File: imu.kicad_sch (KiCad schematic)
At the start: 4 parts

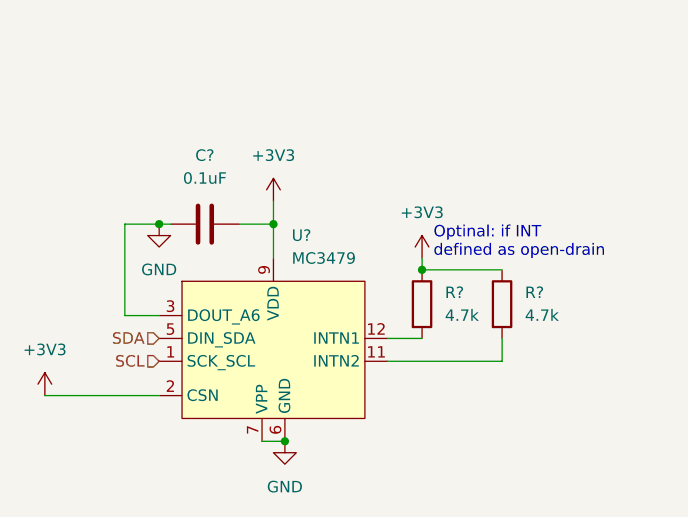
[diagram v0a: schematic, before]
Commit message: Added display, update lora sym, updated usb-pd schematic, connected sd, added external buttons
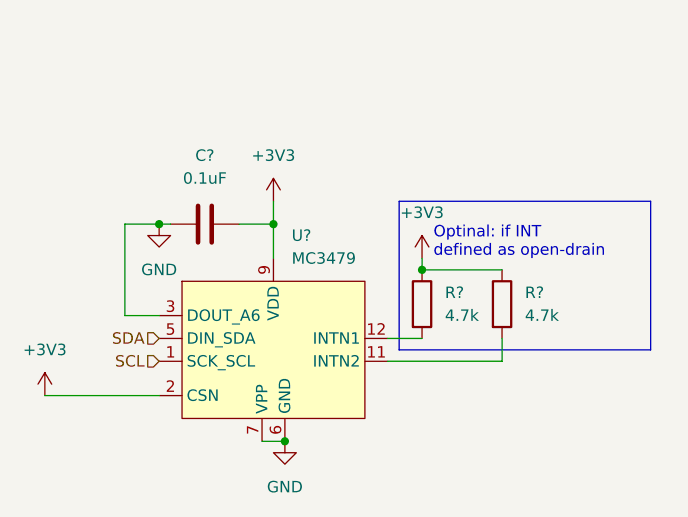
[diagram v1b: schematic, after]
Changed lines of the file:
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@@
+    (stroke (width 0) (type default) (color 0 0 0 0))
+  )
+  (polyline (pts (xy 154.94 81.28) (xy 182.88 81.28))
     (stroke (width 0) (type default) (color 0 0 0 0))
   )
@@
   )
   (wire (pts (xy 124.46 93.98) (xy 124.46 83.82))
+    (stroke (width 0) (type default) (color 0 0 0 0))
+  )
+  (polyline (pts (xy 154.94 81.28) (xy 154.94 97.79))
+    (stroke (width 0) (type default) (color 0 0 0 0))
+  )
+  (polyline (pts (xy 154.94 97.79) (xy 182.88 97.79))
     (stroke (width 0) (type default) (color 0 0 0 0))
   )
@@
     (stroke (width 0) (type default) (color 0 0 0 0))
   )
+  (polyline (pts (xy 182.88 97.79) (xy 182.88 81.28))
+    (stroke (width 0) (type default) (color 0 0 0 0))
+  )

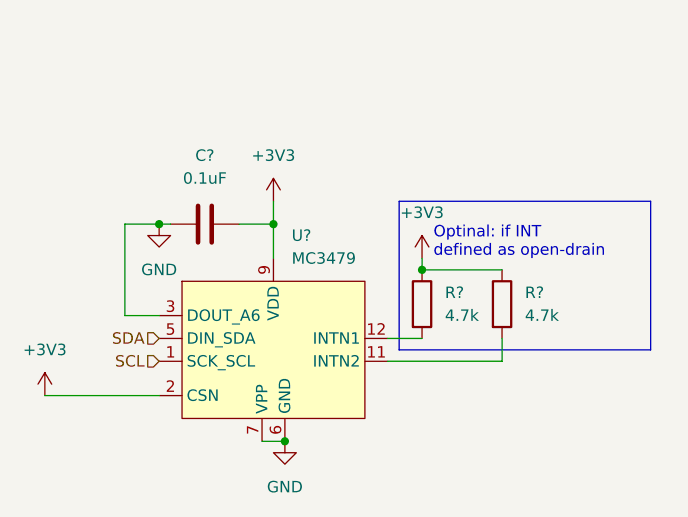
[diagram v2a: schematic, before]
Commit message: added audio ref schematic, added bat to 5V, added shift register, connected devices with other periferals
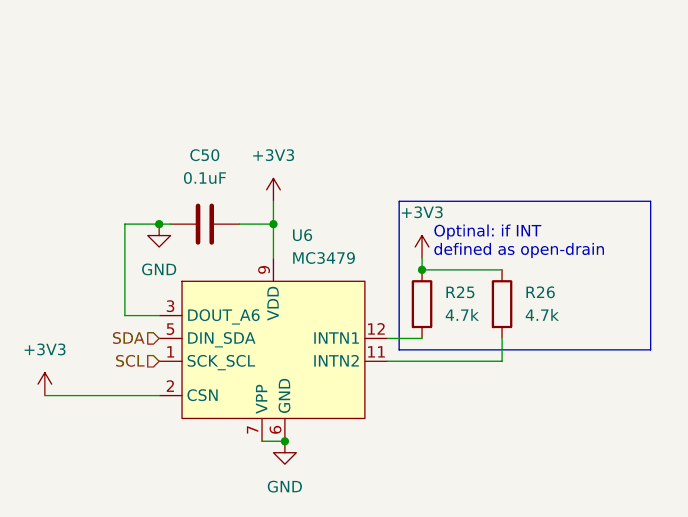
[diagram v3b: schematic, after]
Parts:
- gave numbers to parts that had none: 4
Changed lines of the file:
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@@
   (symbol (lib_id "Device:C") (at 133.35 83.82 90) (unit 1)
     (in_bom yes) (on_board yes) (fields_autoplaced)
-    (property "Reference" "C?" (id 0) (at 133.35 76.2 90))
+    (property "Reference" "C50" (id 0) (at 133.35 76.2 90))
     (property "Value" "0.1uF" (id 1) (at 133.35 78.74 90))
     (property "Footprint" "" (id 2) (at 137.16 82.8548 0)
@@
   (symbol (lib_id "Device:R") (at 157.48 92.71 0) (unit 1)
     (in_bom yes) (on_board yes) (fields_autoplaced)
-    (property "Reference" "R?" (id 0) (at 160.02 91.4399 0)
+    (property "Reference" "R25" (id 0) (at 160.02 91.4399 0)
       (effects (font (size 1.27 1.27)) (justify left))
     )
@@
   (symbol (lib_id "Device:R") (at 166.37 92.71 0) (unit 1)
     (in_bom yes) (on_board yes) (fields_autoplaced)
-    (property "Reference" "R?" (id 0) (at 168.91 91.4399 0)
+    (property "Reference" "R26" (id 0) (at 168.91 91.4399 0)
       (effects (font (size 1.27 1.27)) (justify left))
     )
@@
   (symbol (lib_id "airsoft_controller:MC3479") (at 140.97 97.79 0) (unit 1)
     (in_bom yes) (on_board yes) (fields_autoplaced)
-    (property "Reference" "U?" (id 0) (at 142.9894 85.09 0)
+    (property "Reference" "U6" (id 0) (at 142.9894 85.09 0)
       (effects (font (size 1.27 1.27)) (justify left))
     )

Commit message: added adcin2 config description, fixed some rule check errors
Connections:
- now unconnected: U6.10 (NC), U6.4 (NC), U6.8 (NC)

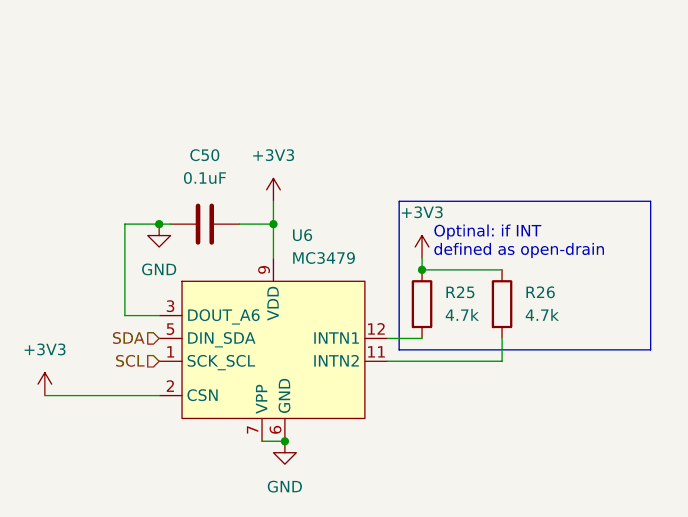
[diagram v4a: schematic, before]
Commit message: minor optimized pinassignement, added capacitors, added connectors
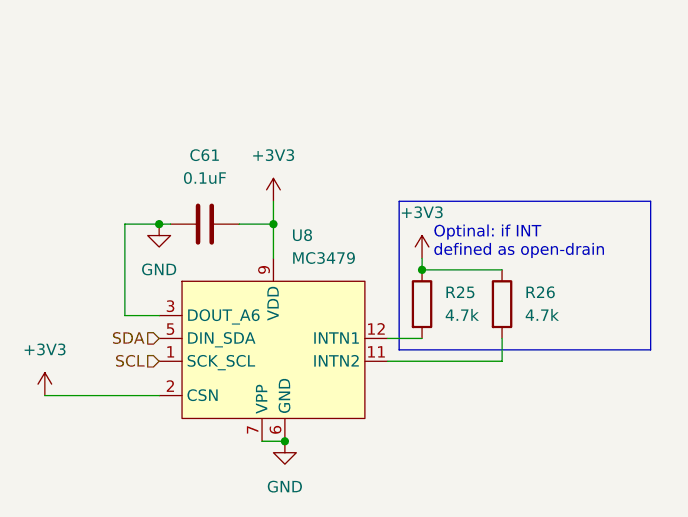
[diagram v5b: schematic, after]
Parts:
- renumbered C50 to C61, U6 to U8
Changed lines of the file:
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@@
   (symbol (lib_id "Device:C") (at 133.35 83.82 90) (unit 1)
     (in_bom yes) (on_board yes) (fields_autoplaced)
-    (property "Reference" "C50" (id 0) (at 133.35 76.2 90))
+    (property "Reference" "C61" (id 0) (at 133.35 76.2 90))
     (property "Value" "0.1uF" (id 1) (at 133.35 78.74 90))
     (property "Footprint" "" (id 2) (at 137.16 82.8548 0)
@@
   (symbol (lib_id "power:+3V3") (at 140.97 81.28 0) (unit 1)
     (in_bom yes) (on_board yes) (fields_autoplaced)
-    (property "Reference" "#PWR0152" (id 0) (at 140.97 85.09 0)
+    (property "Reference" "#PWR071" (id 0) (at 140.97 85.09 0)
       (effects (font (size 1.27 1.27)) hide)
     )
@@
   (symbol (lib_id "power:+3V3") (at 115.57 102.87 0) (unit 1)
     (in_bom yes) (on_board yes) (fields_autoplaced)
-    (property "Reference" "#PWR0155" (id 0) (at 115.57 106.68 0)
+    (property "Reference" "#PWR069" (id 0) (at 115.57 106.68 0)
       (effects (font (size 1.27 1.27)) hide)
     )
@@
   (symbol (lib_id "power:+3V3") (at 157.48 87.63 0) (unit 1)
     (in_bom yes) (on_board yes) (fields_autoplaced)
-    (property "Reference" "#PWR0154" (id 0) (at 157.48 91.44 0)
+    (property "Reference" "#PWR073" (id 0) (at 157.48 91.44 0)
       (effects (font (size 1.27 1.27)) hide)
     )
@@
   (symbol (lib_id "airsoft_controller:MC3479") (at 140.97 97.79 0) (unit 1)
     (in_bom yes) (on_board yes) (fields_autoplaced)
-    (property "Reference" "U6" (id 0) (at 142.9894 85.09 0)
+    (property "Reference" "U8" (id 0) (at 142.9894 85.09 0)
       (effects (font (size 1.27 1.27)) (justify left))
     )
@@
   (symbol (lib_id "power:GND") (at 128.27 83.82 0) (unit 1)
     (in_bom yes) (on_board yes) (fields_autoplaced)
-    (property "Reference" "#PWR0153" (id 0) (at 128.27 90.17 0)
+    (property "Reference" "#PWR070" (id 0) (at 128.27 90.17 0)
       (effects (font (size 1.27 1.27)) hide)
     )
@@
   (symbol (lib_id "power:GND") (at 142.24 107.95 0) (unit 1)
     (in_bom yes) (on_board yes) (fields_autoplaced)
-    (property "Reference" "#PWR0156" (id 0) (at 142.24 114.3 0)
+    (property "Reference" "#PWR072" (id 0) (at 142.24 114.3 0)
       (effects (font (size 1.27 1.27)) hide)
     )

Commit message: PI LC lowpass filter, added CP2012 reset, added connectors
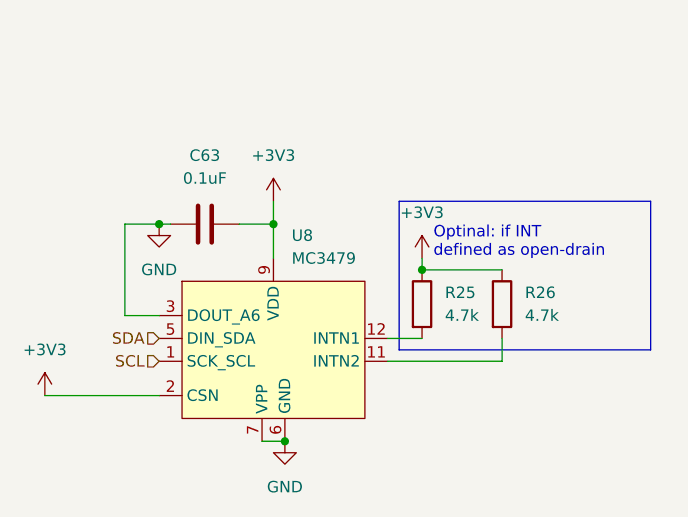
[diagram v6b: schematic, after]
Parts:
- renumbered C61 to C63
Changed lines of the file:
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@@
   (symbol (lib_id "Device:C") (at 133.35 83.82 90) (unit 1)
     (in_bom yes) (on_board yes) (fields_autoplaced)
-    (property "Reference" "C61" (id 0) (at 133.35 76.2 90))
+    (property "Reference" "C63" (id 0) (at 133.35 76.2 90))
     (property "Value" "0.1uF" (id 1) (at 133.35 78.74 90))
     (property "Footprint" "" (id 2) (at 137.16 82.8548 0)
@@
   (symbol (lib_id "power:+3V3") (at 140.97 81.28 0) (unit 1)
     (in_bom yes) (on_board yes) (fields_autoplaced)
-    (property "Reference" "#PWR071" (id 0) (at 140.97 85.09 0)
+    (property "Reference" "#PWR070" (id 0) (at 140.97 85.09 0)
       (effects (font (size 1.27 1.27)) hide)
     )
@@
   (symbol (lib_id "power:+3V3") (at 115.57 102.87 0) (unit 1)
     (in_bom yes) (on_board yes) (fields_autoplaced)
-    (property "Reference" "#PWR069" (id 0) (at 115.57 106.68 0)
+    (property "Reference" "#PWR068" (id 0) (at 115.57 106.68 0)
       (effects (font (size 1.27 1.27)) hide)
     )
@@
   (symbol (lib_id "power:+3V3") (at 157.48 87.63 0) (unit 1)
     (in_bom yes) (on_board yes) (fields_autoplaced)
-    (property "Reference" "#PWR073" (id 0) (at 157.48 91.44 0)
+    (property "Reference" "#PWR072" (id 0) (at 157.48 91.44 0)
       (effects (font (size 1.27 1.27)) hide)
     )
@@
   (symbol (lib_id "power:GND") (at 128.27 83.82 0) (unit 1)
     (in_bom yes) (on_board yes) (fields_autoplaced)
-    (property "Reference" "#PWR070" (id 0) (at 128.27 90.17 0)
+    (property "Reference" "#PWR069" (id 0) (at 128.27 90.17 0)
       (effects (font (size 1.27 1.27)) hide)
     )
@@
   (symbol (lib_id "power:GND") (at 142.24 107.95 0) (unit 1)
     (in_bom yes) (on_board yes) (fields_autoplaced)
-    (property "Reference" "#PWR072" (id 0) (at 142.24 114.3 0)
+    (property "Reference" "#PWR071" (id 0) (at 142.24 114.3 0)
       (effects (font (size 1.27 1.27)) hide)
     )

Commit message: added nfc antenna components, added most of footprints
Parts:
- C63: footprint (none) -> Capacitor_SMD:C_0603_1608Metric_Pad1.08x0.95mm_HandSolder
- R25, R26: footprint (none) -> Resistor_SMD:R_0603_1608Metric_Pad0.98x0.95mm_HandSolder
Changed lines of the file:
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@@
     (property "Reference" "C63" (id 0) (at 133.35 76.2 90))
     (property "Value" "0.1uF" (id 1) (at 133.35 78.74 90))
-    (property "Footprint" "" (id 2) (at 137.16 82.8548 0)
+    (property "Footprint" "Capacitor_SMD:C_0603_1608Metric_Pad1.08x0.95mm_HandSolder" (id 2) (at 137.16 82.8548 0)
       (effects (font (size 1.27 1.27)) hide)
     )
@@
       (effects (font (size 1.27 1.27)) (justify left))
     )
-    (property "Footprint" "" (id 2) (at 155.702 92.71 90)
+    (property "Footprint" "Resistor_SMD:R_0603_1608Metric_Pad0.98x0.95mm_HandSolder" (id 2) (at 155.702 92.71 90)
       (effects (font (size 1.27 1.27)) hide)
     )
@@
       (effects (font (size 1.27 1.27)) (justify left))
     )
-    (property "Footprint" "" (id 2) (at 164.592 92.71 90)
+    (property "Footprint" "Resistor_SMD:R_0603_1608Metric_Pad0.98x0.95mm_HandSolder" (id 2) (at 164.592 92.71 90)
       (effects (font (size 1.27 1.27)) hide)
     )

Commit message: schematic creation
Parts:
- renumbered C63 to C65, R25 to R23, R26 to R24
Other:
- moved on the sheet: C65
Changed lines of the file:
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@@
   (junction (at 157.48 88.9) (diameter 0) (color 0 0 0 0)
   )
-  (junction (at 140.97 83.82) (diameter 0) (color 0 0 0 0)
-  )
-  (junction (at 128.27 83.82) (diameter 0) (color 0 0 0 0)
-  )
   (junction (at 142.24 107.95) (diameter 0) (color 0 0 0 0)
   )
-  (wire (pts (xy 140.97 83.82) (xy 140.97 87.63))
-    (stroke (width 0) (type default) (color 0 0 0 0))
-  )
-  (wire (pts (xy 137.16 83.82) (xy 140.97 83.82))
+  (wire (pts (xy 140.97 86.36) (xy 140.97 87.63))
     (stroke (width 0) (type default) (color 0 0 0 0))
   )
@@
     (stroke (width 0) (type default) (color 0 0 0 0))
   )
-  (wire (pts (xy 124.46 83.82) (xy 128.27 83.82))
-    (stroke (width 0) (type default) (color 0 0 0 0))
-  )
-  (wire (pts (xy 124.46 93.98) (xy 124.46 83.82))
-    (stroke (width 0) (type default) (color 0 0 0 0))
-  )
   (wire (pts (xy 153.67 96.52) (xy 157.48 96.52))
     (stroke (width 0) (type default) (color 0 0 0 0))
@@
     (stroke (width 0) (type default) (color 0 0 0 0))
   )
-  (wire (pts (xy 140.97 81.28) (xy 140.97 83.82))
+  (wire (pts (xy 128.27 87.63) (xy 128.27 93.98))
     (stroke (width 0) (type default) (color 0 0 0 0))
   )
@@
     (stroke (width 0) (type default) (color 0 0 0 0))
   )
-  (wire (pts (xy 128.27 83.82) (xy 129.54 83.82))
-    (stroke (width 0) (type default) (color 0 0 0 0))
-  )
   (wire (pts (xy 139.7 107.95) (xy 142.24 107.95))
     (stroke (width 0) (type default) (color 0 0 0 0))
   )
-  (wire (pts (xy 128.27 93.98) (xy 124.46 93.98))
+  (wire (pts (xy 115.57 87.63) (xy 128.27 87.63))
     (stroke (width 0) (type default) (color 0 0 0 0))
   )
@@
     (effects (font (size 1.27 1.27)) (justify right))
   )
-  (symbol (lib_id "Device:C") (at 133.35 83.82 90) (unit 1)
-    (in_bom yes) (on_board yes) (fields_autoplaced)
-    (property "Reference" "C63" (id 0) (at 133.35 76.2 90))
-    (property "Value" "0.1uF" (id 1) (at 133.35 78.74 90))
-    (property "Footprint" "Capacitor_SMD:C_0603_1608Metric_Pad1.08x0.95mm_HandSolder" (id 2) (at 137.16 82.8548 0)
-      (effects (font (size 1.27 1.27)) hide)
-    )
-    (property "Datasheet" "~" (id 3) (at 133.35 83.82 0)
-      (effects (font (size 1.27 1.27)) hide)
-    )
-    (pin "1")
-    (pin "2")
+  (symbol (lib_id "Device:C") (at 130.81 71.12 180) (unit 1)
+    (in_bom yes) (on_board yes) (fields_autoplaced)
+    (property "Reference" "C65" (id 0) (at 134.62 69.8499 0)
+      (effects (font (size 1.27 1.27)) (justify right))
+    )
+    (property "Value" "0.1uF" (id 1) (at 134.62 72.3899 0)
+      (effects (font (size 1.27 1.27)) (justify right))
+    )
+    (property "Footprint" "Capacitor_SMD:C_0603_1608Metric_Pad1.08x0.95mm_HandSolder" (id 2) (at 129.8448 67.31 0)
+      (effects (font (size 1.27 1.27)) hide)
+    )
+    (property "Datasheet" "~" (id 3) (at 130.81 71.12 0)
+      (effects (font (size 1.27 1.27)) hide)
+    )
+    (pin "1")
+    (pin "2")
+  )
+  (symbol (lib_id "power:+3V3") (at 140.97 86.36 0) (unit 1)
+    (in_bom yes) (on_board yes) (fields_autoplaced)
+    (property "Reference" "#PWR075" (id 0) (at 140.97 90.17 0)
+      (effects (font (size 1.27 1.27)) hide)
+    )
+    (property "Value" "+3V3" (id 1) (at 140.97 81.28 0))
+    (property "Footprint" "" (id 2) (at 140.97 86.36 0)
+      (effects (font (size 1.27 1.27)) hide)
+    )
+    (property "Datasheet" "" (id 3) (at 140.97 86.36 0)
+      (effects (font (size 1.27 1.27)) hide)
+    )
+    (pin "1")
   )
   (symbol (lib_id "Device:R") (at 157.48 92.71 0) (unit 1)
     (in_bom yes) (on_board yes) (fields_autoplaced)
-    (property "Reference" "R25" (id 0) (at 160.02 91.4399 0)
+    (property "Reference" "R23" (id 0) (at 160.02 91.4399 0)
       (effects (font (size 1.27 1.27)) (justify left))
     )
@@
     (pin "2")
   )
-  (symbol (lib_id "power:+3V3") (at 140.97 81.28 0) (unit 1)
-    (in_bom yes) (on_board yes) (fields_autoplaced)
-    (property "Reference" "#PWR070" (id 0) (at 140.97 85.09 0)
-      (effects (font (size 1.27 1.27)) hide)
-    )
-    (property "Value" "+3V3" (id 1) (at 140.97 76.2 0))
-    (property "Footprint" "" (id 2) (at 140.97 81.28 0)
-      (effects (font (size 1.27 1.27)) hide)
-    )
-    (property "Datasheet" "" (id 3) (at 140.97 81.28 0)
+  (symbol (lib_id "power:+3V3") (at 130.81 67.31 0) (unit 1)
+    (in_bom yes) (on_board yes) (fields_autoplaced)
+    (property "Reference" "#PWR073" (id 0) (at 130.81 71.12 0)
+      (effects (font (size 1.27 1.27)) hide)
+    )
+    (property "Value" "+3V3" (id 1) (at 130.81 62.23 0))
+    (property "Footprint" "" (id 2) (at 130.81 67.31 0)
+      (effects (font (size 1.27 1.27)) hide)
+    )
+    (property "Datasheet" "" (id 3) (at 130.81 67.31 0)
       (effects (font (size 1.27 1.27)) hide)
     )
@@
   (symbol (lib_id "power:+3V3") (at 115.57 102.87 0) (unit 1)
     (in_bom yes) (on_board yes) (fields_autoplaced)
-    (property "Reference" "#PWR068" (id 0) (at 115.57 106.68 0)
+    (property "Reference" "#PWR072" (id 0) (at 115.57 106.68 0)
       (effects (font (size 1.27 1.27)) hide)
     )
@@
     (pin "1")
   )
+  (symbol (lib_id "power:GND") (at 115.57 87.63 0) (unit 1)
+    (in_bom yes) (on_board yes) (fields_autoplaced)
+    (property "Reference" "#PWR071" (id 0) (at 115.57 93.98 0)
+      (effects (font (size 1.27 1.27)) hide)
+    )
+    (property "Value" "GND" (id 1) (at 115.57 92.71 0))
+    (property "Footprint" "" (id 2) (at 115.57 87.63 0)
+      (effects (font (size 1.27 1.27)) hide)
+    )
+    (property "Datasheet" "" (id 3) (at 115.57 87.63 0)
+      (effects (font (size 1.27 1.27)) hide)
+    )
+    (pin "1")
+  )
   (symbol (lib_id "Device:R") (at 166.37 92.71 0) (unit 1)
     (in_bom yes) (on_board yes) (fields_autoplaced)
-    (property "Reference" "R26" (id 0) (at 168.91 91.4399 0)
+    (property "Reference" "R24" (id 0) (at 168.91 91.4399 0)
       (effects (font (size 1.27 1.27)) (justify left))
     )
@@
   (symbol (lib_id "power:+3V3") (at 157.48 87.63 0) (unit 1)
     (in_bom yes) (on_board yes) (fields_autoplaced)
-    (property "Reference" "#PWR072" (id 0) (at 157.48 91.44 0)
+    (property "Reference" "#PWR077" (id 0) (at 157.48 91.44 0)
       (effects (font (size 1.27 1.27)) hide)
     )
@@
     (pin "9")
   )
-  (symbol (lib_id "power:GND") (at 128.27 83.82 0) (unit 1)
-    (in_bom yes) (on_board yes) (fields_autoplaced)
-    (property "Reference" "#PWR069" (id 0) (at 128.27 90.17 0)
-      (effects (font (size 1.27 1.27)) hide)
-    )
-    (property "Value" "GND" (id 1) (at 128.27 88.9 0))
-    (property "Footprint" "" (id 2) (at 128.27 83.82 0)
-      (effects (font (size 1.27 1.27)) hide)
-    )
-    (property "Datasheet" "" (id 3) (at 128.27 83.82 0)
-      (effects (font (size 1.27 1.27)) hide)
-    )
-    (pin "1")
-  )
   (symbol (lib_id "power:GND") (at 142.24 107.95 0) (unit 1)
     (in_bom yes) (on_board yes) (fields_autoplaced)
-    (property "Reference" "#PWR071" (id 0) (at 142.24 114.3 0)
+    (property "Reference" "#PWR076" (id 0) (at 142.24 114.3 0)
       (effects (font (size 1.27 1.27)) hide)
     )
@@
       (effects (font (size 1.27 1.27)) hide)
     )
+    (pin "1")
+  )
+  (symbol (lib_id "power:GND") (at 130.81 74.93 0) (unit 1)
+    (in_bom yes) (on_board yes) (fields_autoplaced)
+    (property "Reference" "#PWR074" (id 0) (at 130.81 81.28 0)
+      (effects (font (size 1.27 1.27)) hide)
+    )
+    (property "Value" "GND" (id 1) (at 130.81 80.01 0))
+    (property "Footprint" "" (id 2) (at 130.81 74.93 0)
+      (effects (font (size 1.27 1.27)) hide)
+    )
+    (property "Datasheet" "" (id 3) (at 130.81 74.93 0)
+      (effects (font (size 1.27 1.27)) hide)
+    )
